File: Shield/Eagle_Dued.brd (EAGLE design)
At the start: 115.2 x 89.7 mm, 74 parts, among them IC1 7805TV, IC2 LM340MP-05

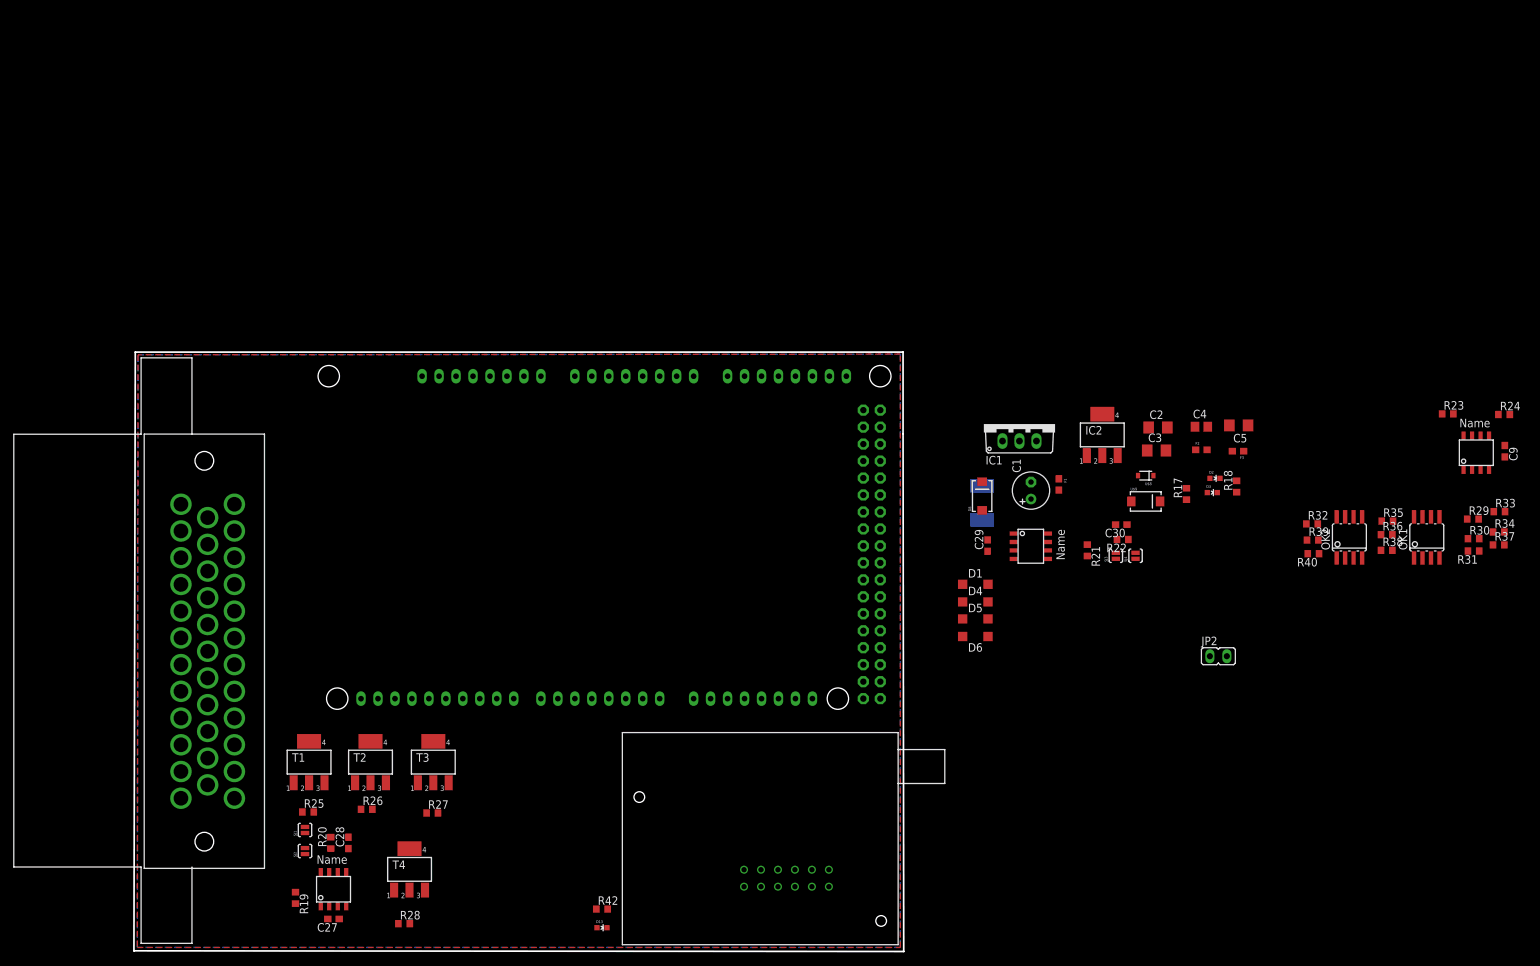
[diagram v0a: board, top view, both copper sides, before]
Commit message: Major redesign of board to encompass the entirety of the case we'd like to use.
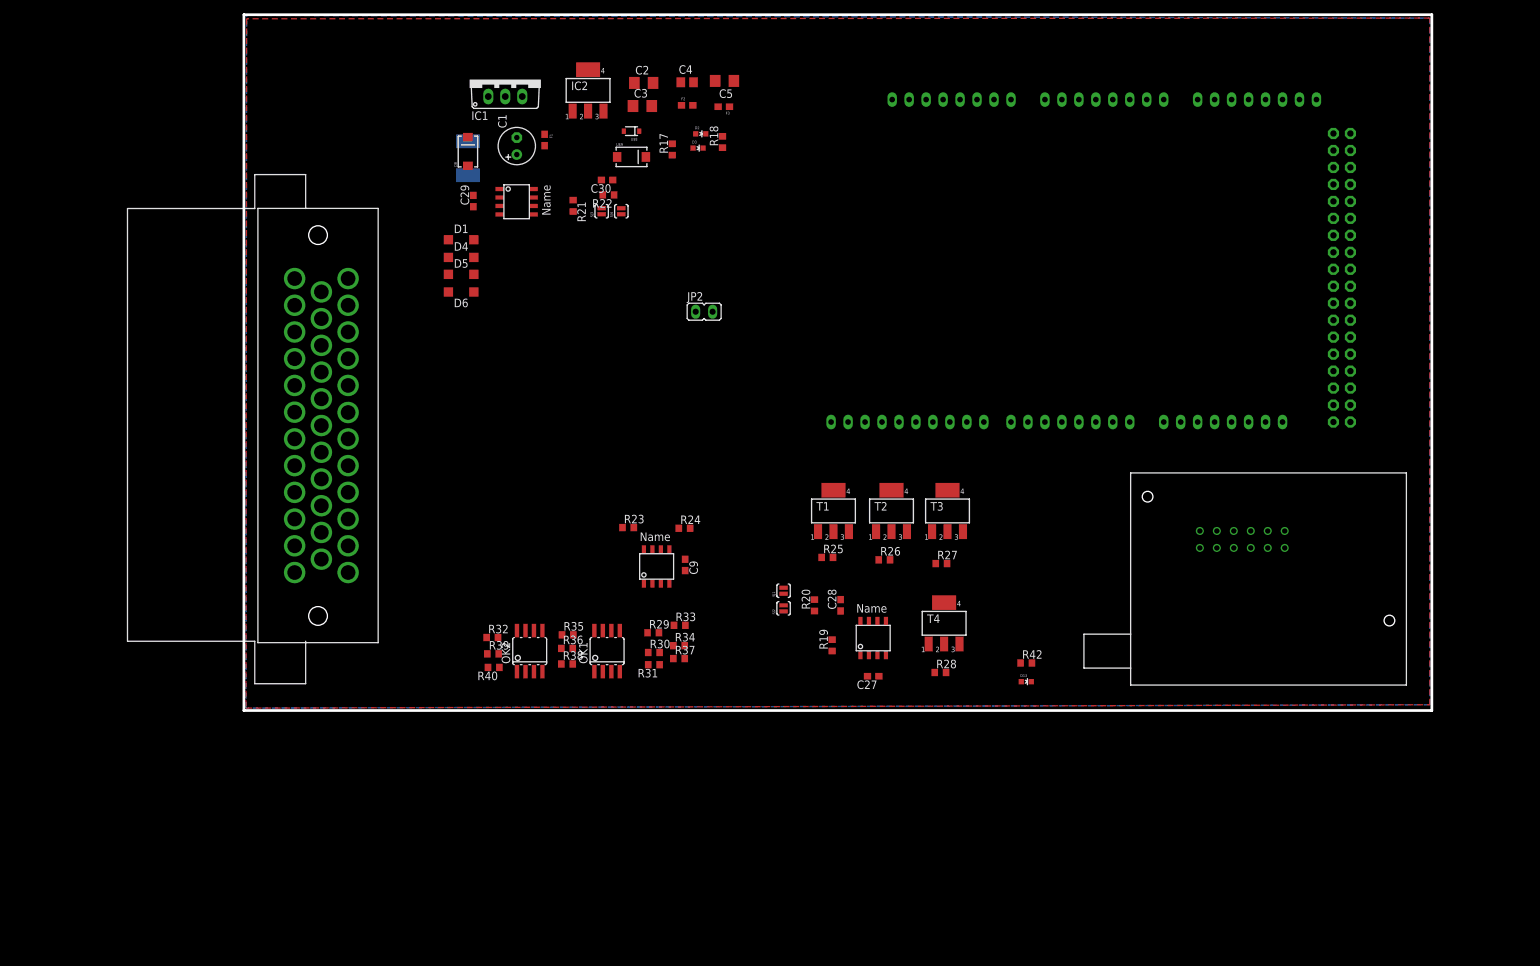
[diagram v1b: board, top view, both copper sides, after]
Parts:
- moved U$4 137.0 mm to (174.0, 35.6), turned to 180 degrees
- moved OK1 123.9 mm to (54.4, 8.89)
- moved R32 123.9 mm to (37.2, 10.9)
- moved U$5 123.9 mm to (59.2, 19.7)
- moved C9 123.9 mm to (66.0, 21.8)
- moved OK2 123.9 mm to (42.8, 8.89)
- moved R23 123.9 mm to (57.5, 27.4)
- moved R33 123.9 mm to (65.2, 12.8)
- moved R34 123.9 mm to (65.1, 9.70)
- moved R37 123.9 mm to (65.1, 7.77)
- moved R39 123.9 mm to (37.3, 8.48)
- moved R24 123.9 mm to (65.9, 27.3)
- moved R29 123.9 mm to (61.3, 11.6)
- moved R30 123.9 mm to (61.4, 8.69)
- moved R31 123.9 mm to (61.4, 6.86)
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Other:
- board size 115.2 x 89.7 mm -> 177.8 x 104.1 mm

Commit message: Updated canbus board to be more correct, fixed size of ampseal connector, totally new DueD board.
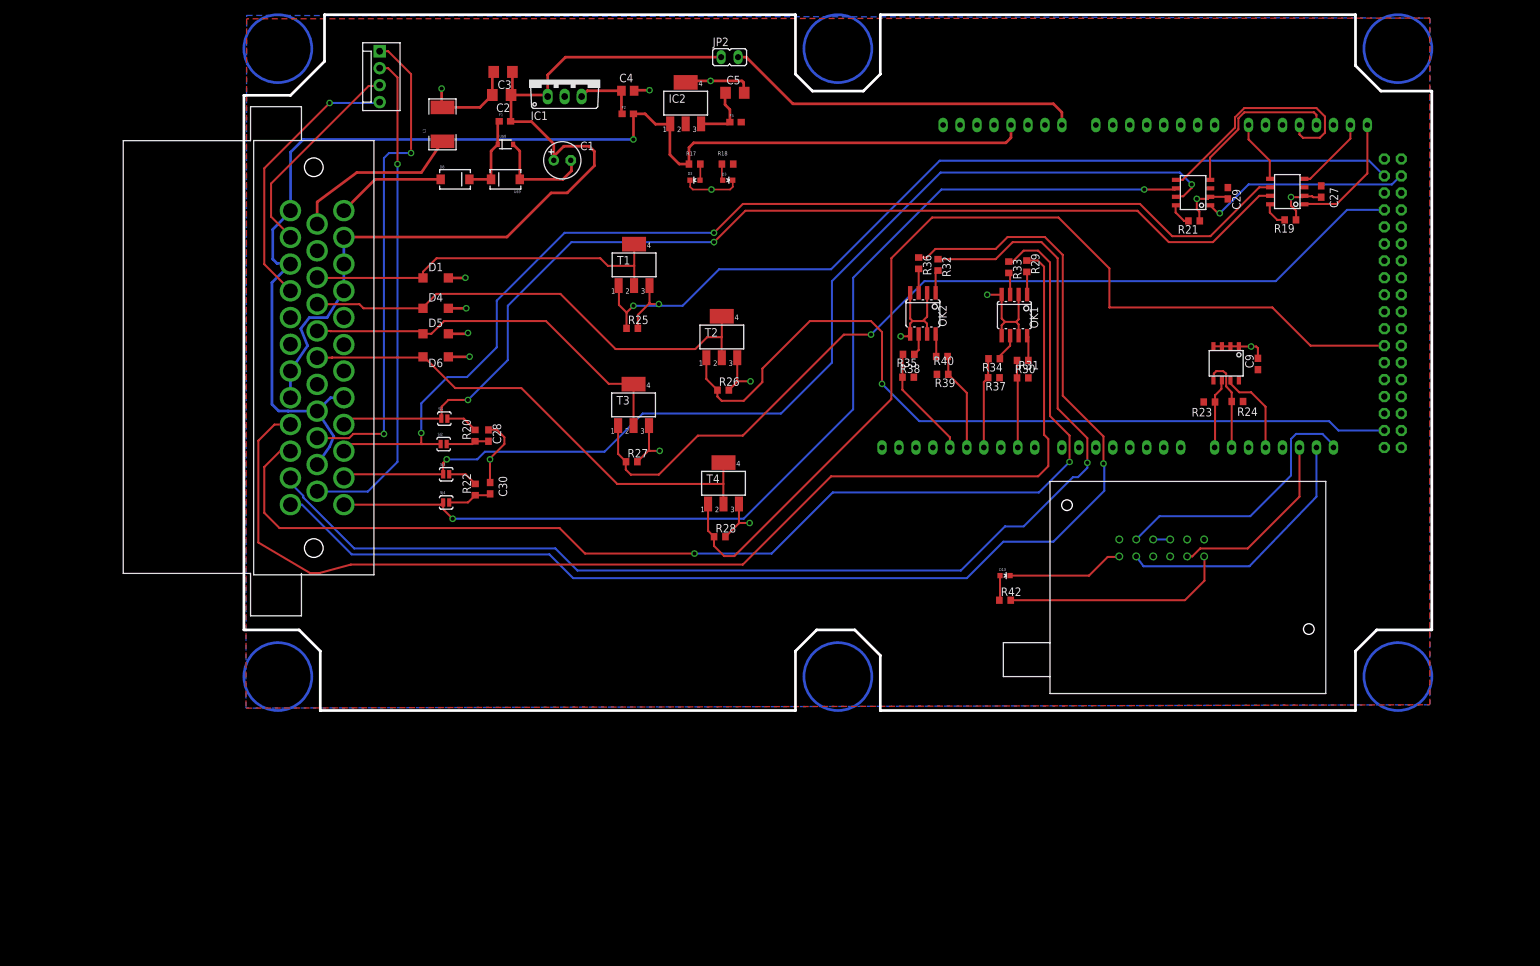
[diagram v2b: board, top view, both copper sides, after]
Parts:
- added JP1: (no value), SparkFun-Connectors:MOLEX-1X4
- moved C29 112.9 mm to (147.3, 77.4), turned to 270 degrees
- moved U$2 105.1 mm to (144.0, 75.0), turned to 90 degrees
- moved C27 98.8 mm to (161.2, 77.7), turned to 270 degrees
- moved U$5 96.6 mm to (149.6, 53.9), turned to 180 degrees
- moved U$6 93.8 mm to (158.1, 75.1), turned to 90 degrees
- moved R19 93.6 mm to (156.6, 73.4), turned to 180 degrees
- moved R21 93.0 mm to (142.2, 73.3), turned to 180 degrees
- moved C9 90.8 mm to (151.8, 51.9), turned to 90 degrees
- moved R23 89.0 mm to (144.5, 46.2)
- moved R32 86.9 mm to (103.9, 66.7), turned to 270 degrees
- moved R24 84.9 mm to (148.7, 46.3), turned to 180 degrees
- moved R40 81.6 mm to (104.5, 53.0), turned to 0 degrees
- moved R39 79.2 mm to (104.6, 50.3), turned to 180 degrees
- moved OK1 79.0 mm to (115.3, 59.2), turned to 180 degrees
- moved R29 78.3 mm to (117.2, 66.5), turned to 270 degrees
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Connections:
- net +12V: now also U$3.3, U$3.30, U$3.31, U$3.4
- net +5V: now also U$3.20, U$3.22, U$3.24, U$3.26, U$3.8; no longer U$3.3
- net AIN1: now also JP1.1, U$3.21; no longer U$3.27
- net AIN2: now also JP1.2, U$3.23; no longer U$3.28
- net AIN3: now also JP1.3, U$3.25; no longer U$3.29
- net AIN4: now also JP1.4, U$3.27; no longer U$3.30
- net CANH0: now also U$3.9; no longer U$3.11
- net CANH1: now also U$3.11; no longer U$3.13
- net CANL0: now also U$3.10; no longer U$3.12
- net CANL1: now also U$3.12; no longer U$3.14
- net DGND: now also U$3.13; no longer U$3.19, U$3.26, U$3.31
- net GND: now also U$3.14, U$3.19, U$3.28, U$3.29, U$3.5, U$3.6, U$3.7
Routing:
- net DIN4: track 0.00 -> 193.6 mm, vias 0 -> 1
- net +5V: track 0.00 -> 187.0 mm, vias 0 -> 1
- net DIN3: track 0.00 -> 185.1 mm, vias 0 -> 1
- net GND: track 0.00 -> 180.5 mm, vias 0 -> 18
- net DIN1: track 0.00 -> 179.9 mm
- net DIN2: track 0.00 -> 179.1 mm, vias 0 -> 2
- net CANL0: track 0.00 -> 169.6 mm, vias 0 -> 2
- net CANH0: track 0.00 -> 162.5 mm, vias 0 -> 2
- net CANL1: track 0.00 -> 158.3 mm, vias 0 -> 2
- net CANH1: track 0.00 -> 158.1 mm, vias 0 -> 2
- net DIGOUT4: track 0.00 -> 152.3 mm
- net DIGOUT3: track 0.00 -> 137.4 mm, vias 0 -> 1
- net +12V: track 0.00 -> 134.2 mm
- net DIGOUT1: track 0.00 -> 130.7 mm, vias 0 -> 1
- net DIGOUT2: track 0.00 -> 124.1 mm, vias 0 -> 1
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- added copper zone on layer 1, net +3V3
- removed copper zone on layer 1, net +5V
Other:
- outline, holes or cut-outs redrawn

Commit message: Additional corrections and goodness for the shields.
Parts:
- added JP3: (no value), jumper:JP1
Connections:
- new net N$1: JP3.1, POWER.5
- net +5V: now also JP3.2; no longer POWER.5
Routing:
- net +5V: track 187.0 -> 158.2 mm
- net N$1: track 0.00 -> 26.1 mm
- net DIGOUT4: track 152.3 -> 151.1 mm

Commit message: Continued finagling with the dued board.
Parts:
- moved U$3 1.78 mm to (13.2, 54.8)
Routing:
- net DIN4: track 193.6 -> 0.00 mm, vias 1 -> 0
- net DIN3: track 185.1 -> 0.00 mm, vias 1 -> 0
- net GND: track 180.5 -> 0.00 mm, vias 18 -> 0
- net DIN1: track 179.9 -> 0.00 mm
- net DIN2: track 179.1 -> 0.00 mm, vias 2 -> 0
- net CANL0: track 169.6 -> 0.00 mm, vias 2 -> 0
- net CANH0: track 162.5 -> 0.00 mm, vias 2 -> 0
- net CANL1: track 158.3 -> 0.00 mm, vias 2 -> 0
- net +5V: track 158.2 -> 0.00 mm, vias 1 -> 0
- net CANH1: track 158.1 -> 0.00 mm, vias 2 -> 0
- net DIGOUT4: track 151.1 -> 0.00 mm
- net DIGOUT3: track 137.4 -> 0.00 mm, vias 1 -> 0
- net +12V: track 134.2 -> 0.00 mm
- net DIGOUT1: track 130.7 -> 0.00 mm, vias 1 -> 0
- net DIGOUT2: track 124.1 -> 0.00 mm, vias 1 -> 0
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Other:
- board size 177.8 x 104.1 mm -> 178.7 x 102 mm

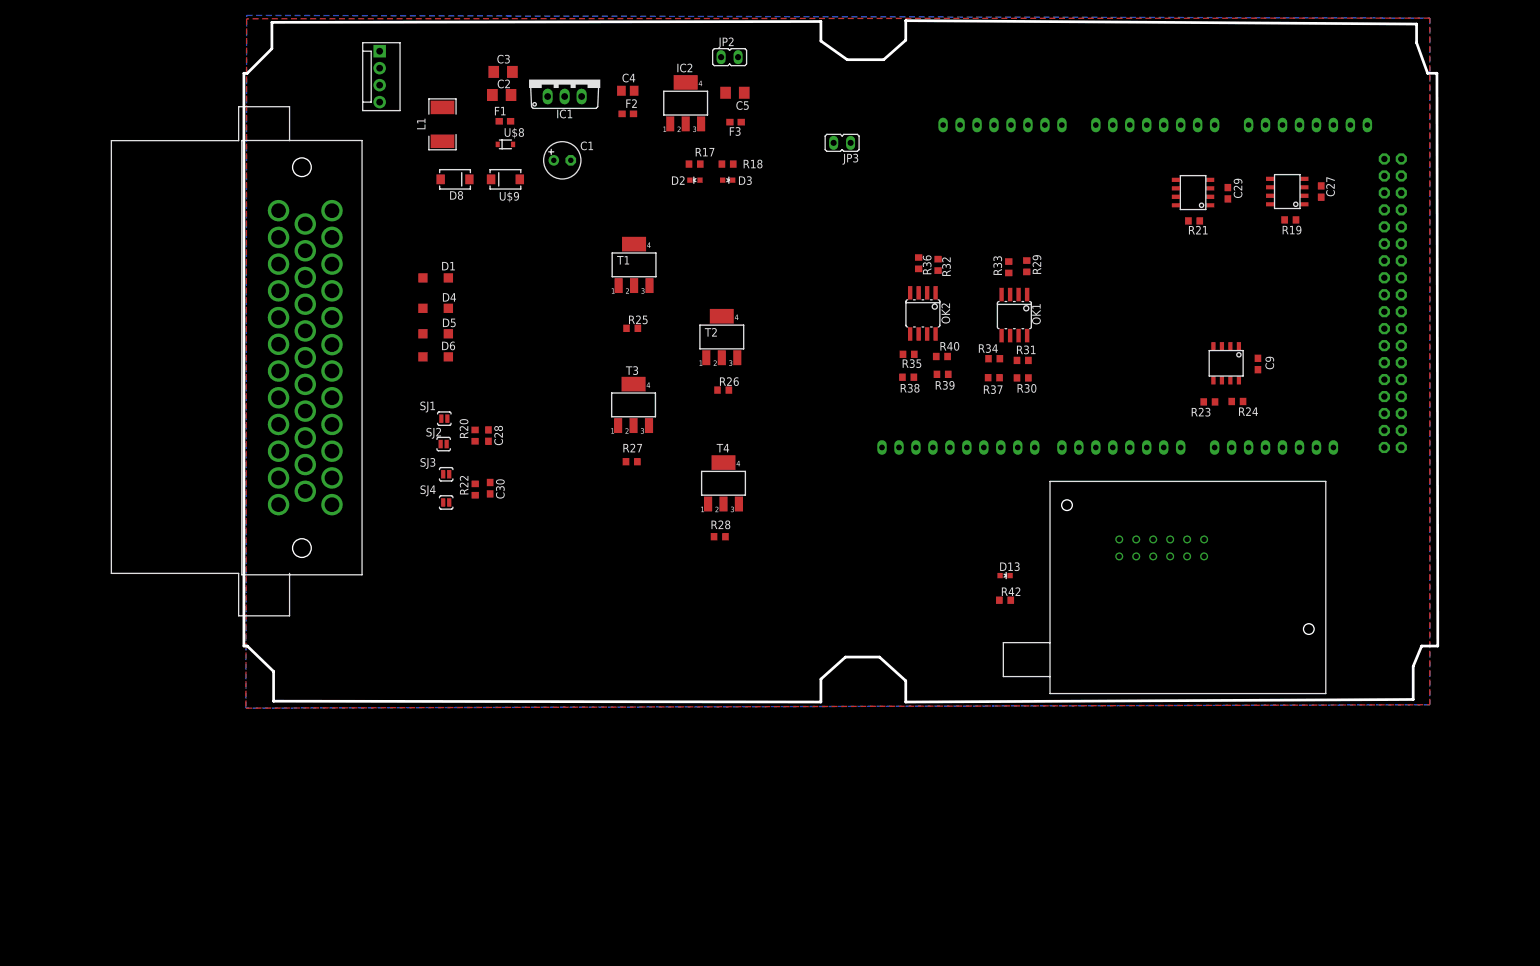
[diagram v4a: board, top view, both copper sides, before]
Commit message: updated dued board to fit a different case.
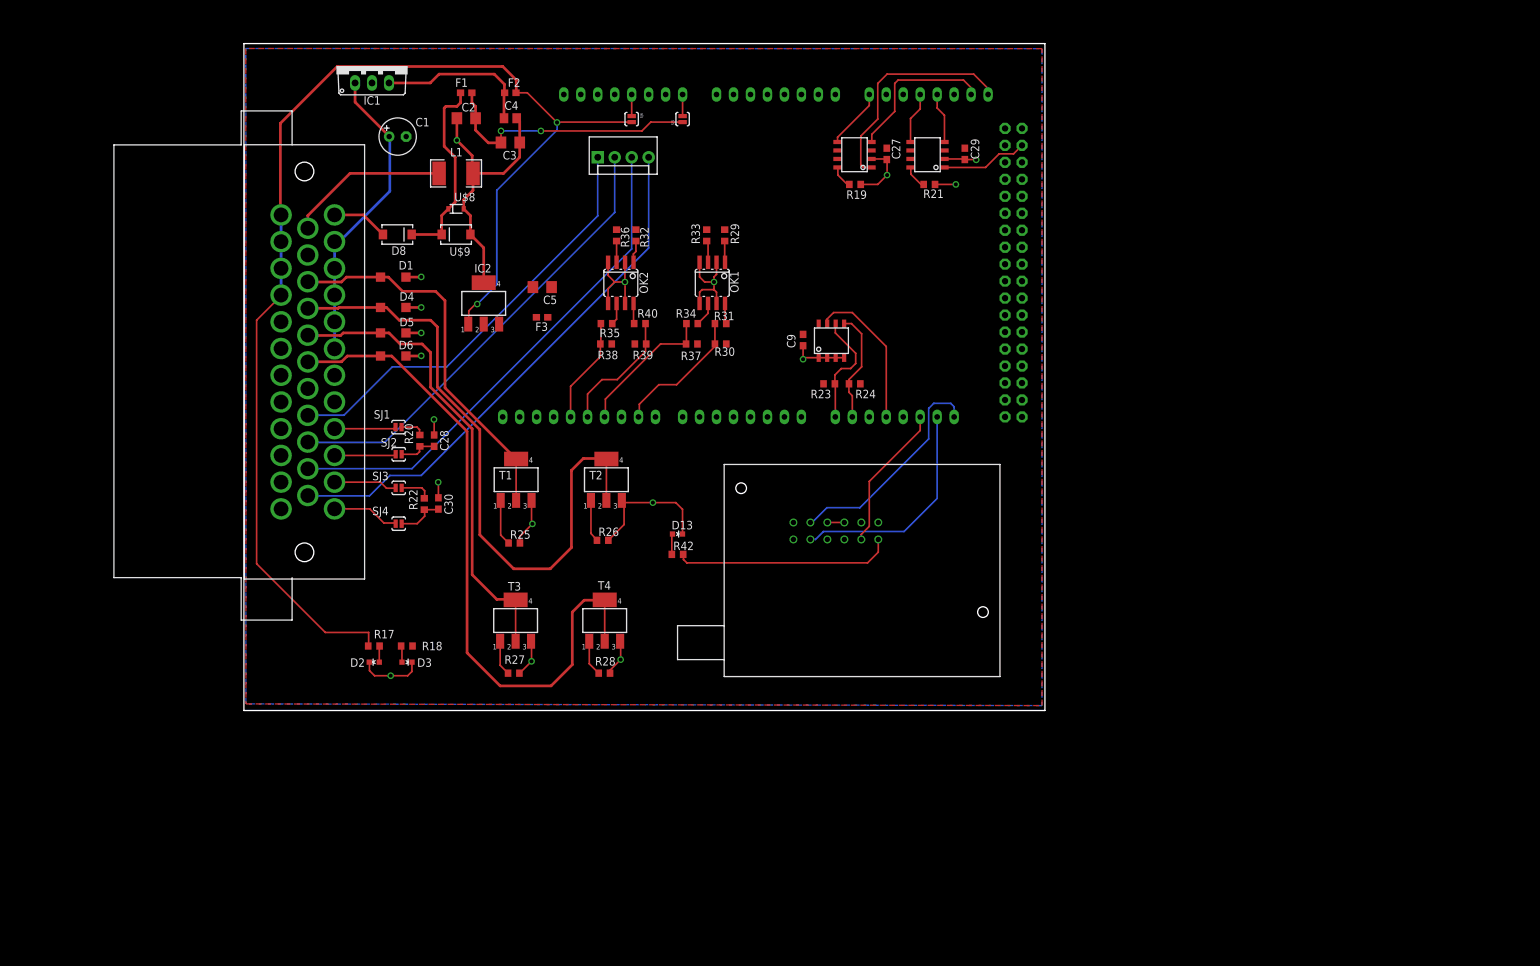
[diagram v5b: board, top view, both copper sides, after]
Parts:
- removed JP2, JP3: (no value), jumper:JP1
- added SJ5, SJ6: SOLDERJUMPERNO, SparkFun-Passives:SJ_2S-NO
- moved D2 86.6 mm to (19.5, 7.24)
- moved D3 86.6 mm to (24.4, 7.24)
- moved R17 86.6 mm to (19.5, 9.65)
- moved R18 86.6 mm to (24.4, 9.65)
- moved C9 68.2 mm to (83.7, 55.4), turned to 270 degrees
- moved R19 65.4 mm to (91.5, 78.7)
- moved C27 65.3 mm to (96.2, 83.3)
- moved U$6 65.0 mm to (93.3, 80.6)
- moved U$5 64.2 mm to (85.4, 53.4), turned to 0 degrees
- moved R24 57.3 mm to (91.4, 48.9)
- moved R23 57.0 mm to (87.6, 48.9)
- moved ADCH 57.0 mm to (102.5, 92.2)
- moved PWML 57.0 mm to (74.5, 43.9)
- moved XIO 57.0 mm to (115.2, 65.5)
- moved POWER 57.0 mm to (56.8, 92.2)
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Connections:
- new net +5V\: U$3.28
- net +12V: now also SJ5.1, U$3.5, U$3.6; no longer JP2.1, U$3.30, U$3.31
- net +5V: now also SJ6.2, U$3.25, U$3.27; no longer JP3.2, U$3.20, U$3.22, U$3.8
- net AIN1: now also U$3.20; no longer U$3.21
- net AIN2: now also U$3.21; no longer U$3.23
- net AIN3: now also U$3.22; no longer U$3.25
- net AIN4: now also U$3.23; no longer U$3.27
- net GND: now also U$3.30, U$3.31, U$3.8; no longer U$3.28, U$3.5, U$3.6
- net N$1: now also SJ6.1; no longer JP3.1
- net VIN: now also SJ5.2; no longer JP2.2
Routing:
- net +5V: track 0.00 -> 186.9 mm, vias 0 -> 2
- net GND: track 0.00 -> 158.8 mm, vias 0 -> 18
- net MOSFET4: track 0.00 -> 100.8 mm
- net MOSFET2: track 0.00 -> 95.9 mm
- net +12V: track 0.00 -> 85.7 mm, vias 0 -> 2
- net AIN4: track 0.00 -> 80.0 mm
- net AIN3: track 0.00 -> 75.8 mm
- net MOSFET3: track 0.00 -> 69.9 mm
- net AIN2: track 0.00 -> 68.5 mm
- net AIN1: track 0.00 -> 64.5 mm
- net MOSFET1: track 0.00 -> 56.6 mm
- net CANTX0: track 0.00 -> 33.9 mm
- net RXD3: track 0.00 -> 33.7 mm
- net TXD3: track 0.00 -> 33.3 mm
- net N$4: track 0.00 -> 32.7 mm
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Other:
- board size 178.7 x 102 mm -> 119.9 x 99.8 mm
